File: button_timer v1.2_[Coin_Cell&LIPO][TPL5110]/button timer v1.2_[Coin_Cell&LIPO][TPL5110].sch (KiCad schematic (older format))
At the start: 27 parts, among them J1 Conn_01x05_Female, Q1 TSM2301ACX, SW1 SW_Push, SW2 SW_Push, U1 TPS61097A, U2 AP2112K-3.3, U3 TPL5110, X1 ESP-12E

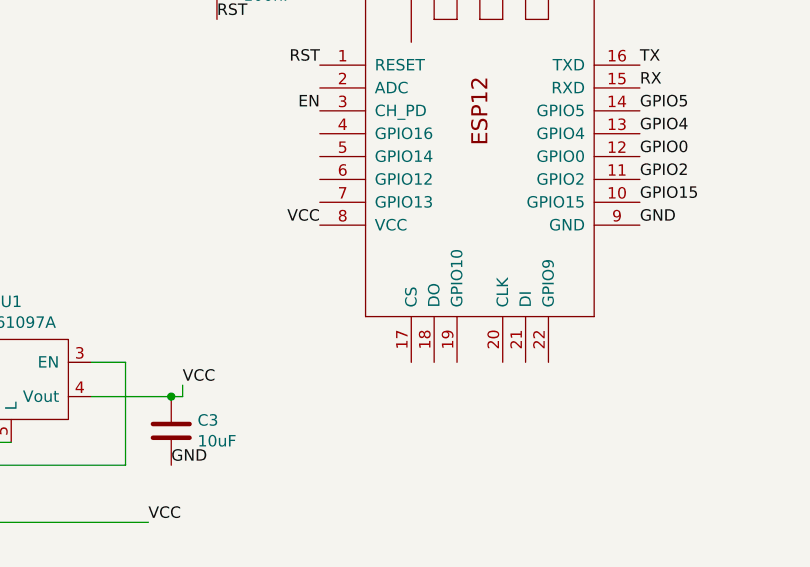
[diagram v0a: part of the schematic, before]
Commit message: cap between esp vcc and ground added
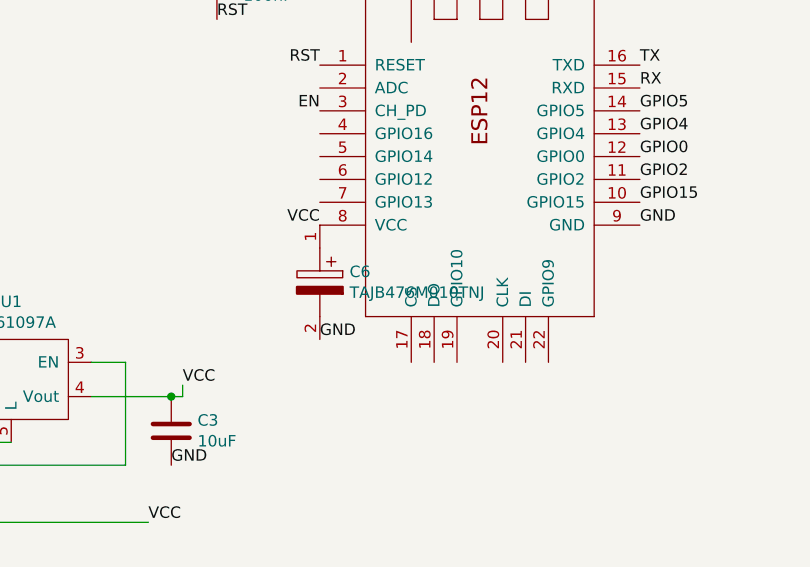
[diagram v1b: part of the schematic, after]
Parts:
- added C6: TAJB476M010TNJ, CAPPM3528X210N, symbol SamacSys_Parts:TAJB476M010TNJ
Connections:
- net GND: now also C6.2
- net VCC: now also C6.1
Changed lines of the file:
@@
 Wire Wire Line
 	3200 4600 3800 4600
+$Comp
+L SamacSys_Parts:TAJB476M010TNJ C6
+U 1 1 60364890
+P 5300 3700
+F 0 "C6" V 5504 3830 50  0000 L CNN
+F 1 "TAJB476M010TNJ" V 5595 3830 50  0000 L CNN
+F 2 "CAPPM3528X210N" H 5650 3750 50  0001 L CNN
+F 3 "http://datasheets.avx.com/TAJ.pdf" H 5650 3650 50  0001 L CNN
+F 4 "Tantalum Capacitors - Solid SMD 10volts 47uF 20%" H 5650 3550 50  0001 L CNN "Description"
+F 5 "2.1" H 5650 3450 50  0001 L CNN "Height"
+F 6 "AVX" H 5650 3350 50  0001 L CNN "Manufacturer_Name"
+F 7 "TAJB476M010TNJ" H 5650 3250 50  0001 L CNN "Manufacturer_Part_Number"
+F 8 "581-TAJB476M010TNJ" H 5650 3150 50  0001 L CNN "Mouser Part Number"
+F 9 "https://www.mouser.co.uk/ProductDetail/AVX/TAJB476M010TNJ?qs=pYVYkI7xuRVorIKKgcxm0A%3D%3D" H 5650 3050 50  0001 L CNN "Mouser Price/Stock"
+F 10 "TAJB476M010TNJ" H 5650 2950 50  0001 L CNN "Arrow Part Number"
+F 11 "https://www.arrow.com/en/products/tajb476m010tnj/avx" H 5650 2850 50  0001 L CNN "Arrow Price/Stock"
+	1    5300 3700
+	0    1    1    0
+$EndComp
+Text Label 5300 4200 0    50   ~ 0
+GND
 $EndSCHEMATC

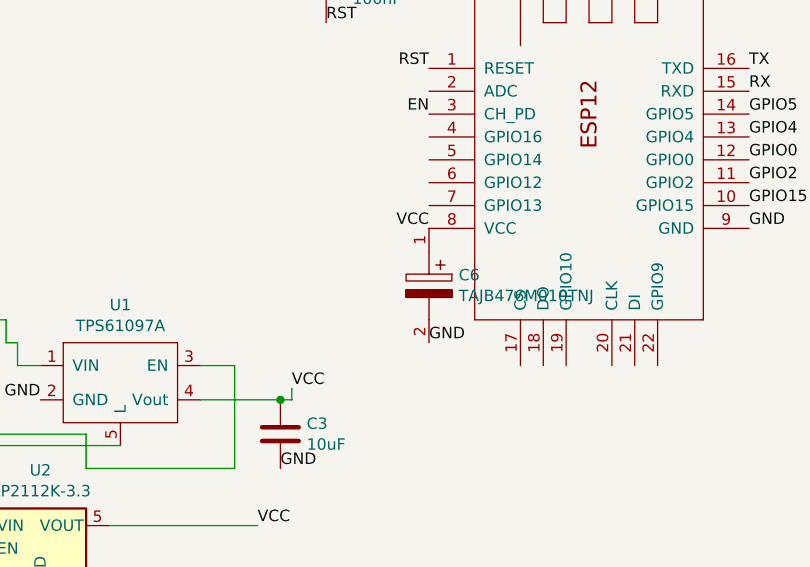
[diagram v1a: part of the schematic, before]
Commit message: Added 100nF decoupling capacitors between VCC and Ground of the ESP
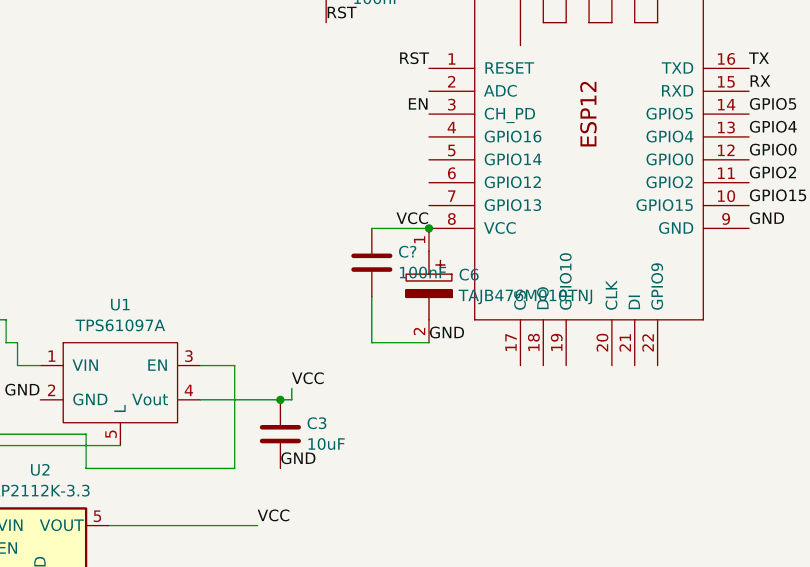
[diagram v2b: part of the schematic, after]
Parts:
- added C?: 100nF, handsolder:C_0402_1005Metric_Pad0.74x0.62mm_HandSoldermod, symbol Device:C
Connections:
- net GND: now also C?.2
- net VCC: now also C?.1
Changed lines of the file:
@@
 Text Label 5300 4200 0    50   ~ 0
 GND
+$Comp
+L Device:C C?
+U 1 1 6036880A
+P 5050 3850
+F 0 "C?" H 5165 3896 50  0000 L CNN
+F 1 "100nF" H 5165 3805 50  0000 L CNN
+F 2 "handsolder:C_0402_1005Metric_Pad0.74x0.62mm_HandSoldermod" H 5088 3700 50  0001 C CNN
+F 3 "~" H 5050 3850 50  0001 C CNN
+	1    5050 3850
+	1    0    0    -1
+$EndComp
+Wire Wire Line
+	5050 3700 5300 3700
+Connection ~ 5300 3700
+Wire Wire Line
+	5050 4000 5050 4200
+Wire Wire Line
+	5050 4200 5300 4200
 $EndSCHEMATC
